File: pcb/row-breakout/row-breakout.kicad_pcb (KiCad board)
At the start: 2 copper layers, 30.9 x 34.4 mm, 4 parts, among them J1 AudioJack4_SwitchTR1, J2 Conn_01x02, J3 RJ45, J4 Conn_01x08

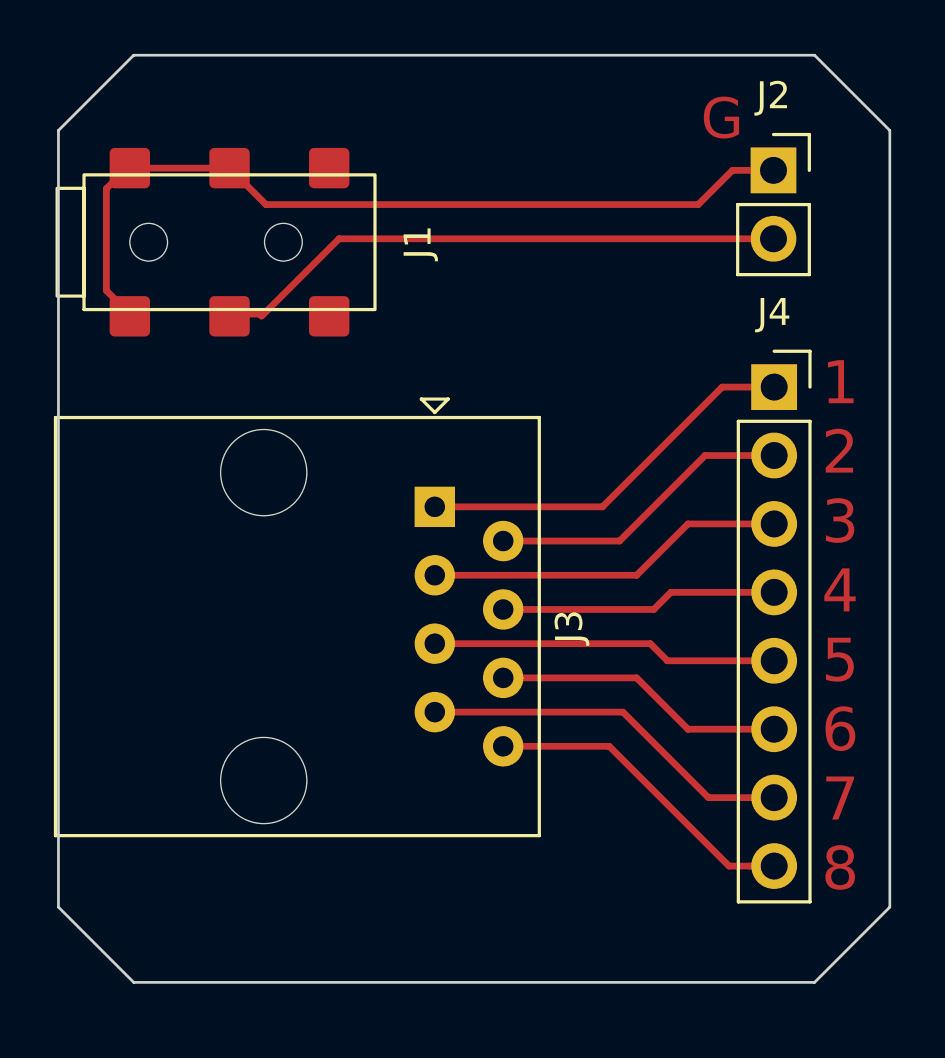
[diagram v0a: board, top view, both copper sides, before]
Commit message: Flip RJ45 on Row Breakout for Single Side Board
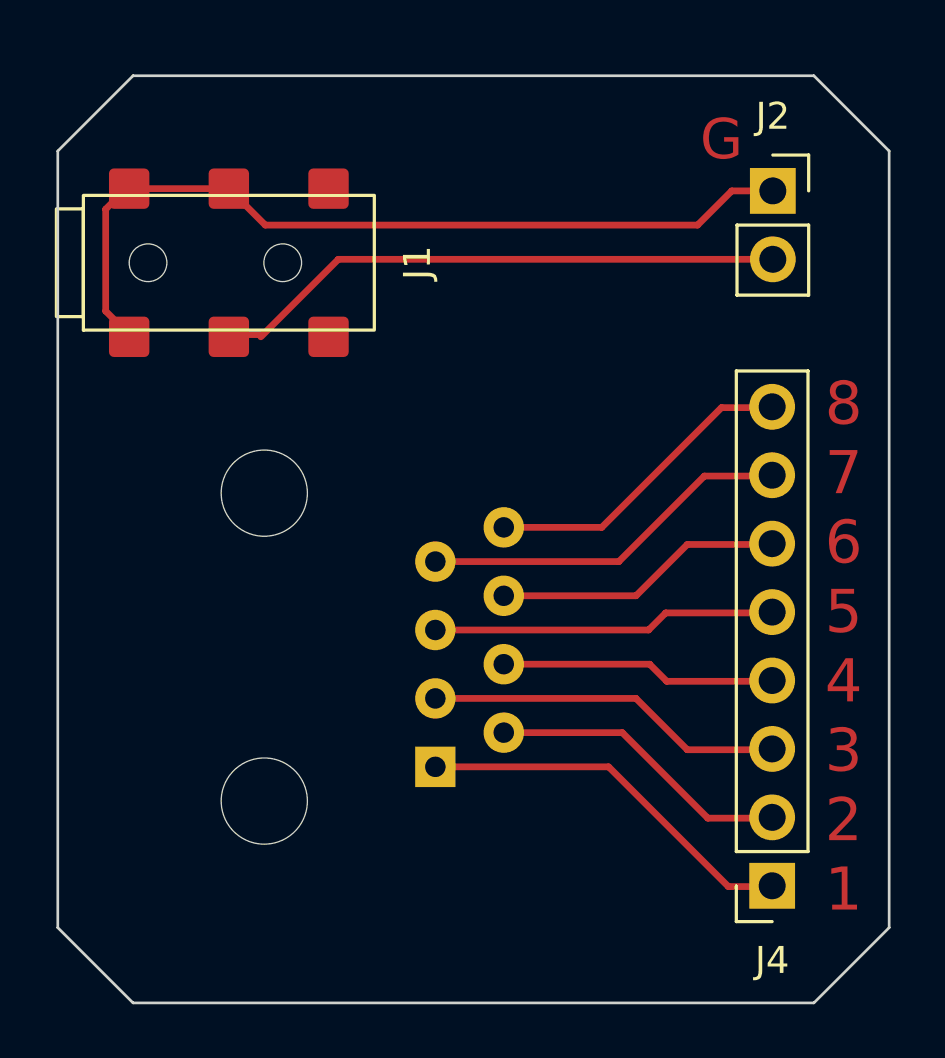
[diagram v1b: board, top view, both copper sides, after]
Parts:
- J3: moved to B.Cu
- moved J4 18.5 mm to (47.4, 54.6), turned to 180 degrees
- moved J3 9.65 mm to (34.9, 50.2), turned to 90 degrees
- moved J1 0.76 mm to (27.3, 31.5)
- moved J2 0.76 mm to (47.5, 28.8)
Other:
- board text added: "8 7 6 5 4 3 2 1"
- board text removed: "1 2 3 4 5 6 7 8"

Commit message: Create Gerbers
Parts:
- added H1: MountingHole, MountingHole:MountingHole_2.7mm_M2.5, F.Cu at (40.5, 34.3)
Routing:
- net Net-(J1-PadT): track 21.4 -> 22.1 mm
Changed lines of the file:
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@@
       (outputformat 1)
       (mirror false)
-      (drillshape 1)
+      (drillshape 0)
       (scaleselection 1)
-      (outputdirectory "")
+      (outputdirectory "Gerbers/")
     )
   )
@@
     (pad "TN" smd roundrect (at -2.75 3.7 90) (size 1.5 1.5) (layers "F.Cu" "F.Paste" "F.Mask") (roundrect_rratio 0.125)
       (net 12 "unconnected-(J1-PadTN)") (pintype "passive+no_connect"))
+  )
+  (footprint "MountingHole:MountingHole_2.7mm_M2.5" (layer "F.Cu")
+    (at 40.513 34.29)
+    (descr "Mounting Hole 2.7mm, no annular, M2.5")
+    (tags "mounting hole 2.7mm no annular m2.5")
+    (property "Sheetfile" "row-breakout.kicad_sch")
+    (property "Sheetname" "")
+    (attr exclude_from_pos_files)
+    (fp_text reference "H1" (at 0 -3.7) (layer "F.SilkS")
+      (effects (font (size 1 1) (thickness 0.15)))
+    )
+    (fp_text value "MountingHole" (at 0 3.7) (layer "F.Fab")
+      (effects (font (size 1 1) (thickness 0.15)))
+    )
+    (fp_text user "${REFERENCE}" (at 0.3 0) (layer "F.Fab")
+      (effects (font (size 1 1) (thickness 0.15)))
+    )
+    (fp_circle (center 0 0) (end 2.7 0) (layer "Cmts.User") (width 0.15) (fill none))
+    (fp_circle (center 0 0) (end 2.95 0) (layer "F.CrtYd") (width 0.05) (fill none))
+    (pad "" np_thru_hole circle locked (at 0 0) (size 2.7 2.7) (drill 2.7) (layers *.Cu *.Mask))
   )
   (footprint "Connector_PinSocket_2.54mm:PinSocket_1x02_P2.54mm_Vertical" (layer "F.Cu")
@@
     (effects (font (size 1.5 1.5) (thickness 0.25)))
   )
-  (segment (start 31.344 31.325) (end 28.467 34.202) (width 0.25) (layer "F.Cu") (net 1))
-  (segment (start 47.473 31.325) (end 31.344 31.325) (width 0.25) (layer "F.Cu") (net 1))
+  (segment (start 44.958 30.48) (end 32.189 30.48) (width 0.25) (layer "F.Cu") (net 1))
+  (segment (start 32.189 30.48) (end 28.467 34.202) (width 0.25) (layer "F.Cu") (net 1))
+  (segment (start 47.473 31.325) (end 45.803 31.325) (width 0.25) (layer "F.Cu") (net 1))
+  (segment (start 45.803 31.325) (end 44.958 30.48) (width 0.25) (layer "F.Cu") (net 1))
   (segment (start 28.467 34.119) (end 27.28 34.119) (width 0.25) (layer "F.Cu") (net 1))
+  (segment (start 28.321 28.702) (end 29.718 27.305) (width 0.25) (layer "F.Cu") (net 2))
   (segment (start 23.58 28.702) (end 27.28 28.702) (width 0.25) (layer "F.Cu") (net 2))
-  (segment (start 45.949 28.785) (end 47.473 28.785) (width 0.25) (layer "F.Cu") (net 2))
   (segment (start 23.205479 28.993521) (end 23.58 28.619) (width 0.25) (layer "F.Cu") (net 2))
+  (segment (start 29.718 27.305) (end 44.571568 27.305) (width 0.25) (layer "F.Cu") (net 2))
   (segment (start 23.58 34.119) (end 22.708 33.247) (width 0.25) (layer "F.Cu") (net 2))
   (segment (start 22.708 29.464) (end 23.553 28.619) (width 0.25) (layer "F.Cu") (net 2))
-  (segment (start 28.633 30.055) (end 44.679 30.055) (width 0.25) (layer "F.Cu") (net 2))
-  (segment (start 44.679 30.055) (end 45.949 28.785) (width 0.25) (layer "F.Cu") (net 2))
-  (segment (start 27.28 28.702) (end 28.633 30.055) (width 0.25) (layer "F.Cu") (net 2))
+  (segment (start 44.571568 27.305) (end 46.051568 28.785) (width 0.25) (layer "F.Cu") (net 2))
+  (segment (start 46.051568 28.785) (end 47.473 28.785) (width 0.25) (layer "F.Cu") (net 2))
+  (segment (start 27.28 28.702) (end 28.321 28.702) (width 0.25) (layer "F.Cu") (net 2))
   (segment (start 22.708 33.247) (end 22.708 29.464) (width 0.25) (layer "F.Cu") (net 2))
   (segment (start 23.553 28.619) (end 23.58 28.619) (width 0.25) (layer "F.Cu") (net 2))

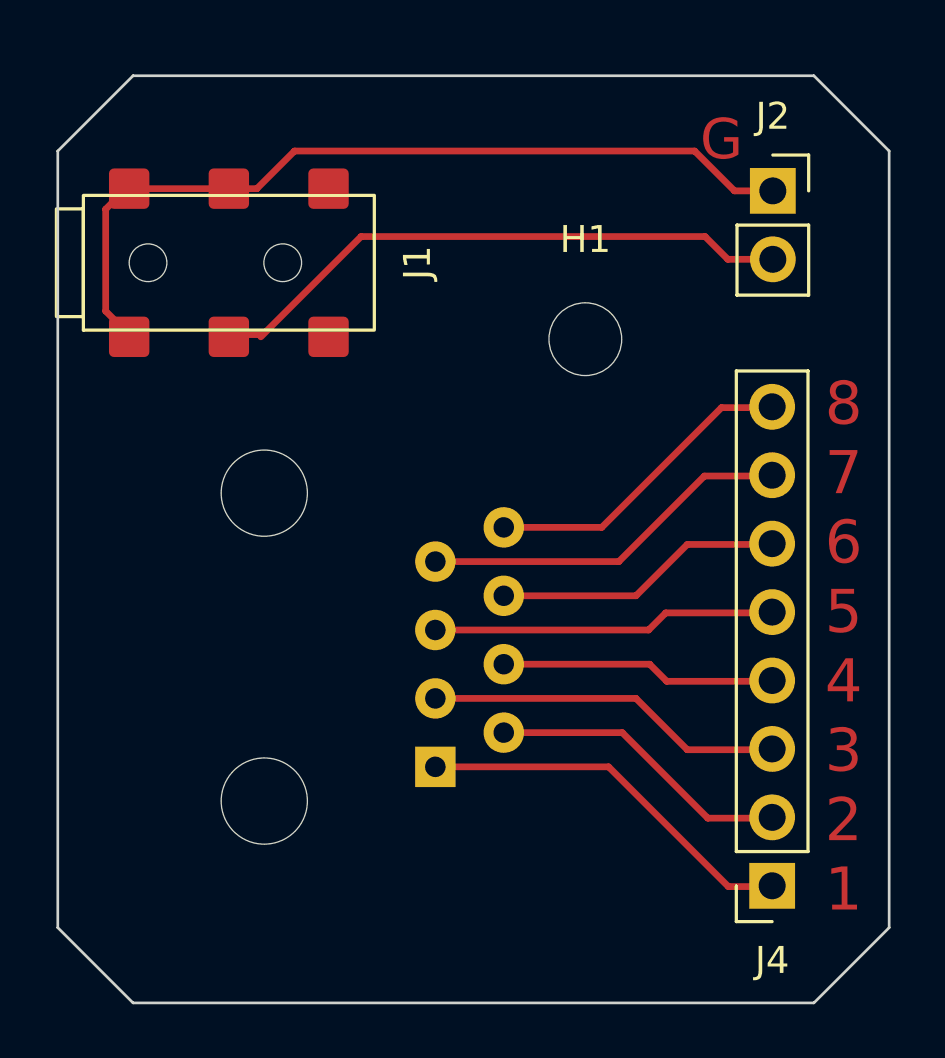
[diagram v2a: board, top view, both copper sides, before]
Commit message: Add Grounded Copper Fills to Row Breakout and Main Board
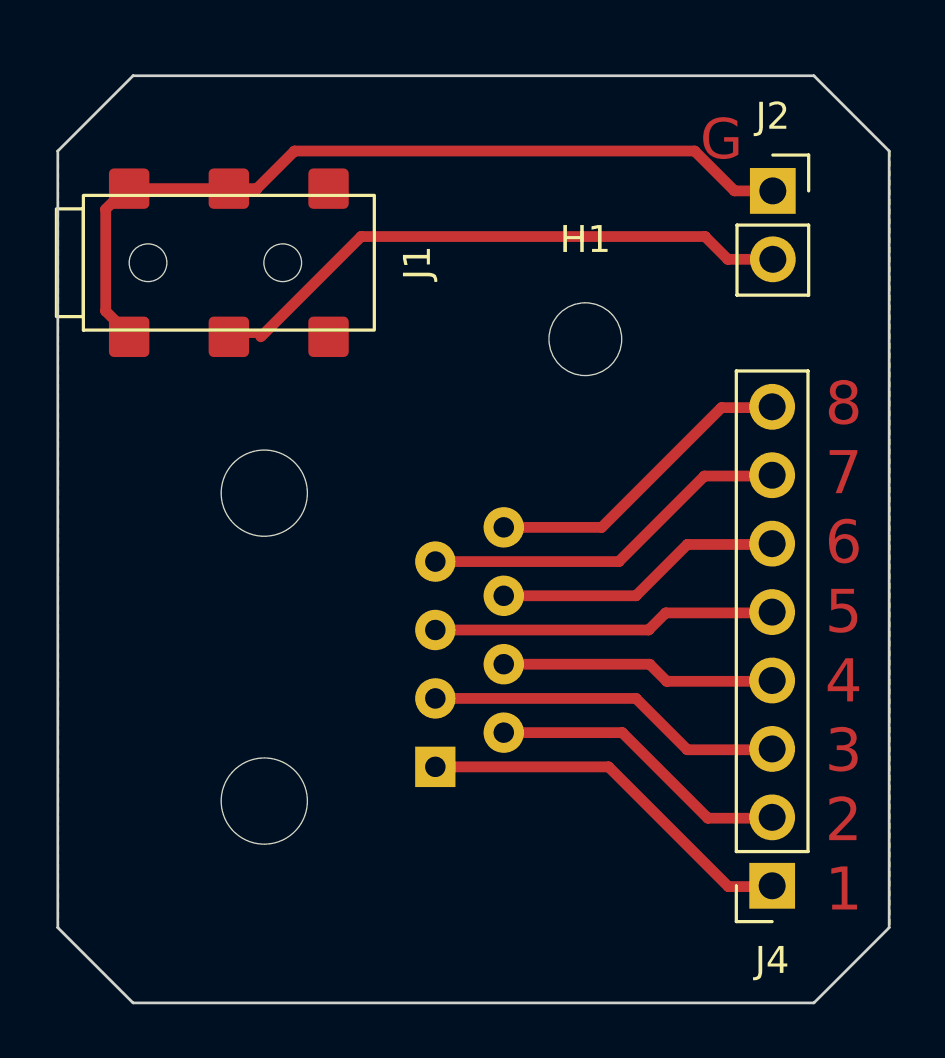
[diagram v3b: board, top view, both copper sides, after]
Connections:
- net Net-(J1-PadR1) renamed Earth
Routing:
- added copper zone on B.Cu, net Earth
- added copper zone on F.Cu, net Earth
